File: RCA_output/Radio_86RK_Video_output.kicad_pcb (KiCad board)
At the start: 2 copper layers, 45.2 x 21.1 mm, 10 parts, among them J1 VIDEO_OUT, J2 Conn_01x04_Pin, Q1 2N3904

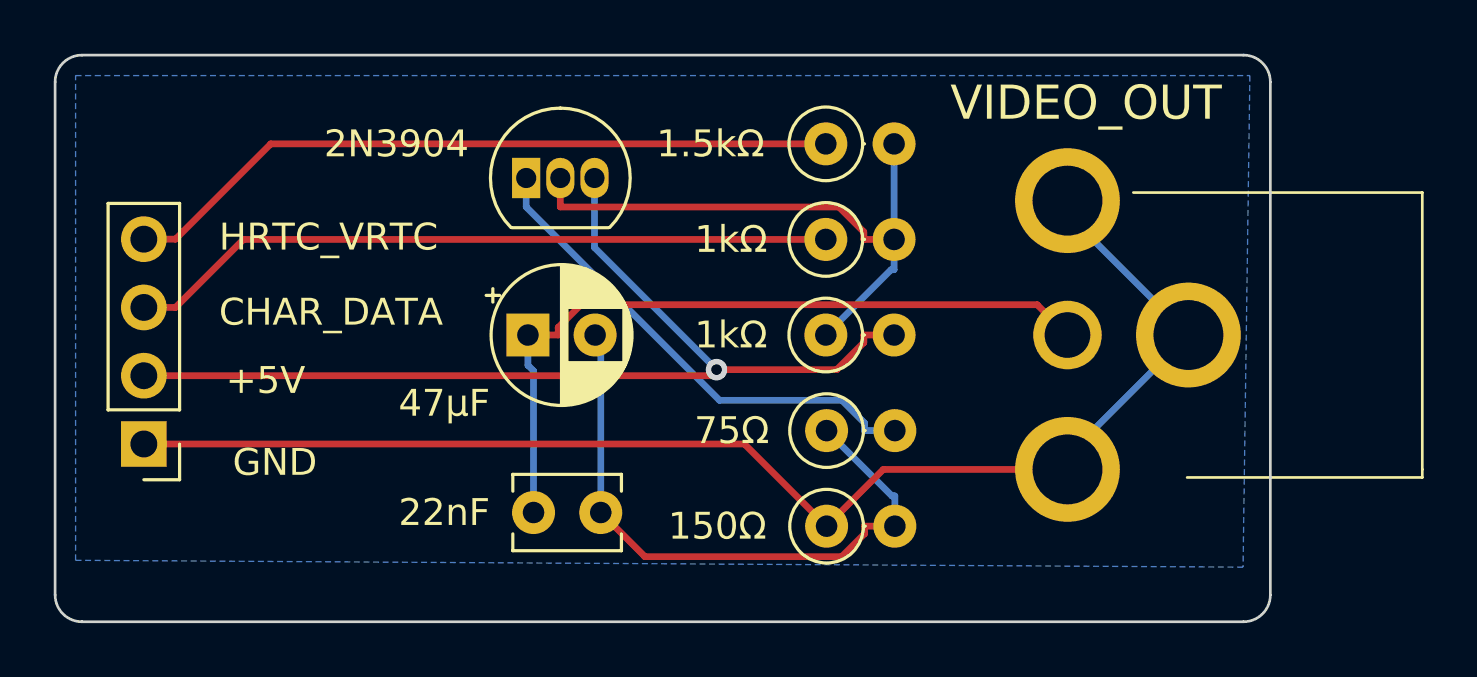
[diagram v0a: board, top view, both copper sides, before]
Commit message: Added mounting hole
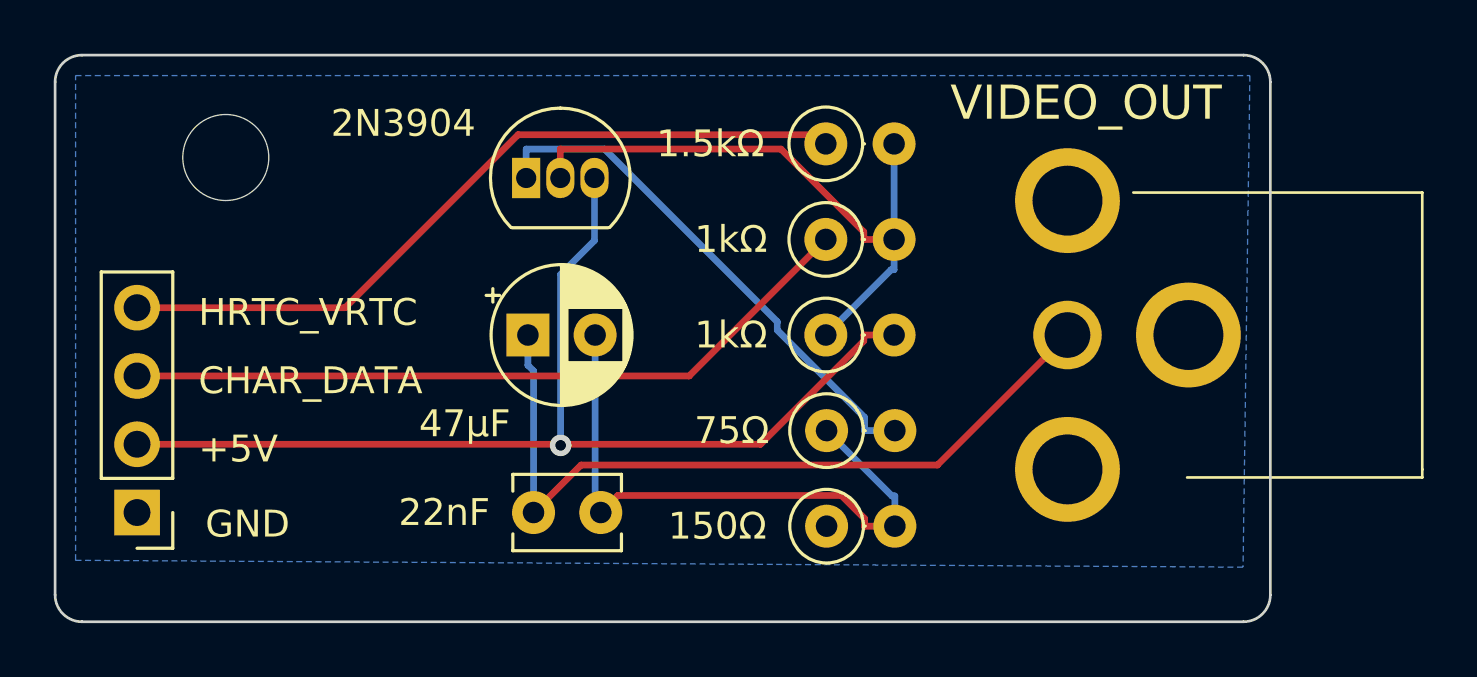
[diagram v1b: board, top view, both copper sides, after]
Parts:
- added H1: MountingHole, MountingHole:MountingHole_3.2mm_M3, F.Cu at (110.2, 70.4)
- moved J2 2.56 mm to (106.9, 83.6)
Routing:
- net GND: track 50.2 -> 0.00 mm
- net 5V: track 37.7 -> 40.5 mm
- net HRTC_VRTC: track 26.8 -> 28.4 mm
- net Net-(J1-Signal): track 27.9 -> 29.3 mm
- net CHAR_DATA: track 26.4 -> 27.7 mm
- net Net-(Q1-E): track 18.4 -> 19.6 mm
- net Net-(Q1-B): track 22.4 -> 23.3 mm

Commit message: Changed HRTC_VRTC to CRTC
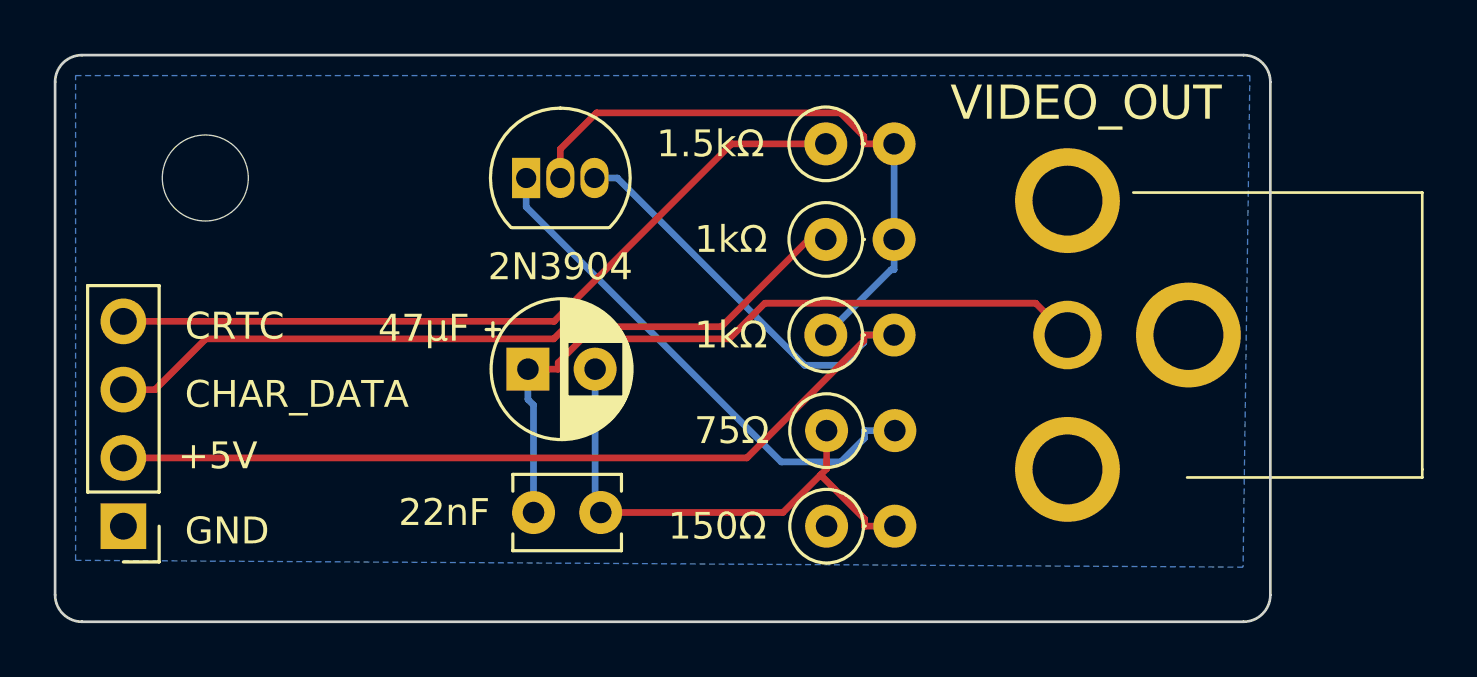
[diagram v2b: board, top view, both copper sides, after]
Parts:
- moved C2 1.27 mm to (121.5, 78.2)
- moved H1 1.08 mm to (109.5, 71.1)
- moved J2 0.72 mm to (106.4, 84.1)
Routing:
- net 5V: track 40.5 -> 45.4 mm, vias 1 -> 0
- net Net-(C1-Pad1): track 23.2 -> 19.6 mm
- net Net-(J1-Signal): track 29.3 -> 27.1 mm
- net CHAR_DATA: track 27.7 -> 28.4 mm
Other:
- board text added: "CRTC"
- board text removed: "HRTC_VRTC"
